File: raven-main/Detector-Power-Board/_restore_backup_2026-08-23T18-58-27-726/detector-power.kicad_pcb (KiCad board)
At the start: 2 copper layers, 37 x 52.5 mm, 38 parts, among them J1 DeployLipo, J2 Conn_01x04, J9 UCLipo, U1 LT8330IS6-TRMPBF, U2 TPS22810DRV, U3 LM317LCLPRE3, U4 LM317LCLPRE3

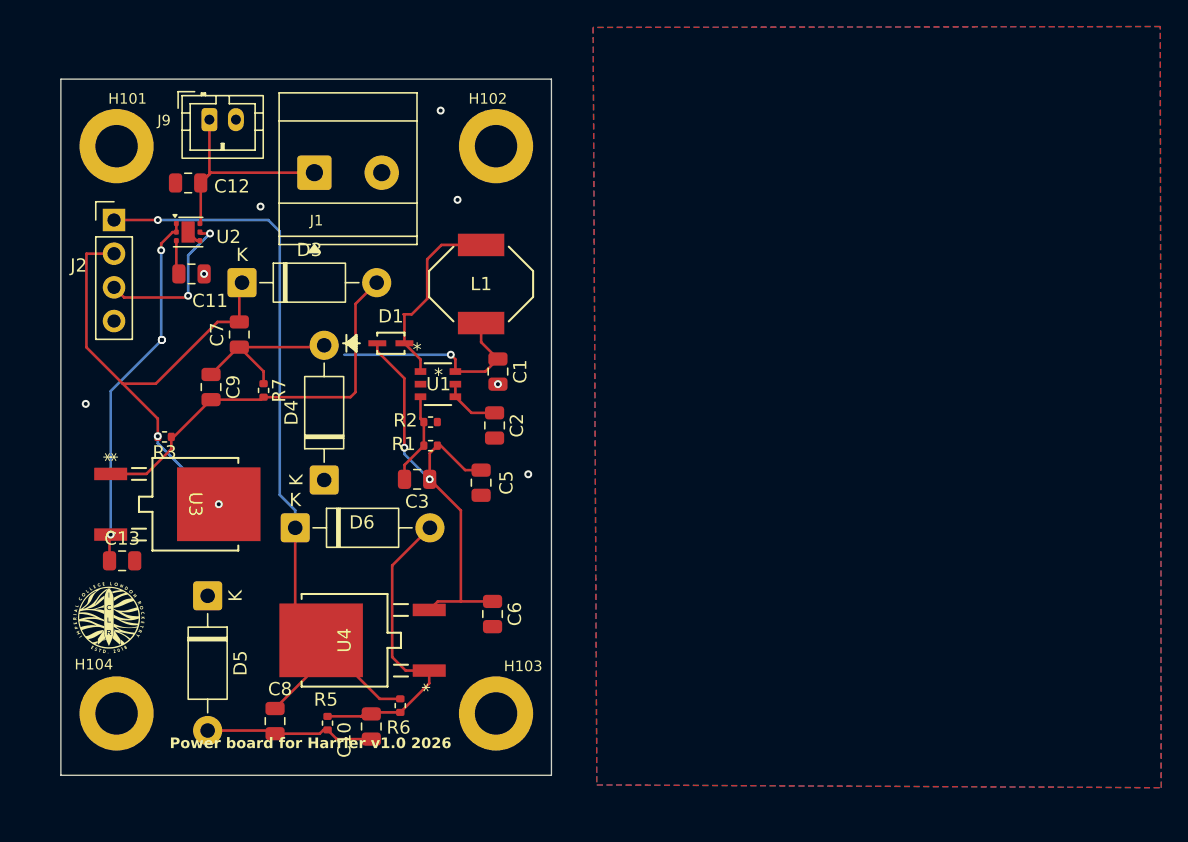
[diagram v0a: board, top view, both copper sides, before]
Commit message: Replaced LDO with correct one
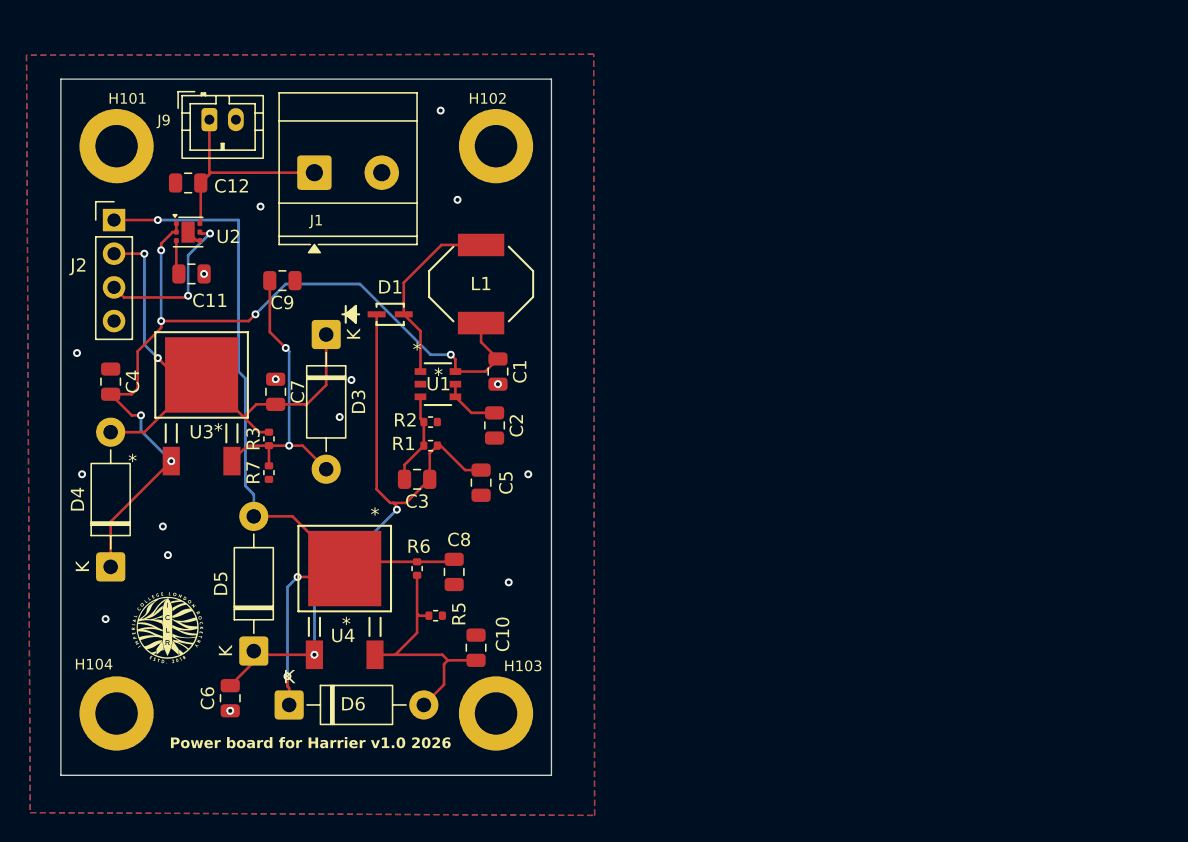
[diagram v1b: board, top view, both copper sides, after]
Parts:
- removed C13: 0.1u, Capacitor_SMD:C_0805_2012Metric
- added C4: 0.1u, Capacitor_SMD:C_0805_2012Metric, F.Cu at (114.6, 80.3)
- U3, U4: footprint LM317MDT_TR:DPAK_STM -> LM317AMDTNOPB:TD03B_TEX
- moved C6 20.8 mm to (123.6, 104.1), turned to 90 degrees
- moved C8 17.6 mm to (140.5, 94.6)
- moved D4 17.4 mm to (114.6, 94.2)
- moved G*** 17.3 mm to (122.5, 85.0)
- moved D6 13.4 mm to (128.0, 104.6)
- moved R5 11.5 mm to (139.1, 97.9), turned to 180 degrees
- moved R6 10.4 mm to (137.7, 94.4), turned to 90 degrees
- moved C10 9.89 mm to (142.1, 100.3), turned to -90 degrees
- moved U3 9.76 mm to (121.4, 79.8), turned to 0 degrees
- moved C9 9.67 mm to (127.5, 72.6), turned to 180 degrees
- moved R3 7.88 mm to (126.5, 84.6), turned to 90 degrees
- moved D3 7.46 mm to (130.8, 76.7), turned to -90 degrees
- moved R7 6.21 mm to (126.5, 87.1), turned to 90 degrees
- moved D5 5.43 mm to (125.3, 100.6), turned to 90 degrees
- moved U4 5.41 mm to (132.2, 94.4), turned to 0 degrees
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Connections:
- C10 pad 1: Net-(D5-A) -> GND
- C6 pad 1: /Power_Out_27.5V -> GND
- C6 pad 2: GND -> /Power_Out_27.5V
- C7 pad 1: Net-(D4-A) -> GND
- C8 pad 1: Net-(D5-A) -> GND
- C9 pad 1: Net-(D4-A) -> GND
- D4 pad 1: GND -> /BBIN
- D4 pad 2: Net-(D4-A) -> /Power_Out_5V
- D5 pad 1: GND -> /Power_Out_27.5V
- D5 pad 2: Net-(D5-A) -> /Filtered_Power_Out_25V
- R5 pad 1: Net-(D6-A) -> GND
- R5 pad 2: Net-(D5-A) -> Net-(D6-A)
- R6 pad 1: /Filtered_Power_Out_25V -> Net-(D6-A)
- R6 pad 2: Net-(D6-A) -> /Filtered_Power_Out_25V
- R7 pad 1: Net-(D4-A) -> GND
- U3 pad 1: Net-(D3-A) -> /BBIN
- U3 pad 2: /BBIN -> /Power_Out_5V
- U3 pad 3: /Power_Out_5V -> Net-(D3-A)
- U4 pad 1: Net-(D6-A) -> /Power_Out_27.5V
- U4 pad 2: /Power_Out_27.5V -> /Filtered_Power_Out_25V
- U4 pad 3: /Filtered_Power_Out_25V -> Net-(D6-A)
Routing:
- net /BBIN: track 44.0 -> 66.7 mm
- net /Power_Out_27.5V: track 34.2 -> 47.4 mm
- net Net-(D4-A): track 13.0 -> 0.00 mm
- net Net-(D5-A): track 12.8 -> 0.00 mm
- net Net-(D3-A): track 30.5 -> 22.9 mm, vias 0 -> 2
- net Net-(D6-A): track 23.8 -> 19.5 mm
- net /Filtered_Power_Out_25V: track 59.4 -> 63.1 mm, vias 1 -> 3
- net /Power_Out_5V: track 38.9 -> 41.0 mm, vias 3 -> 2
- net GND: vias 7 -> 17
